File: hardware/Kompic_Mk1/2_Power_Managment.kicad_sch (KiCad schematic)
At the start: 32 parts, among them SW1 SKSCLBE010, U16 TPS62840DLCR, U2 XC6206P182MR, U4 BQ25619RTWR

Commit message: Added Circuit page! Minor touchups to schematic + Schematic PDF.
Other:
- company: Ivan Porupski May2026(c) -> Ivan Porupski June2026(c)
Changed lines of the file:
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@@
 	(paper "A4")
 	(title_block
-		(date "2026-05-30")
-		(rev "iv7.0")
-		(company "Ivan Porupski May2026(c)")
+		(date "2026-06-02")
+		(rev "iv7.1")
+		(company "Ivan Porupski June2026(c)")
 	)
 	(text "right at pin"

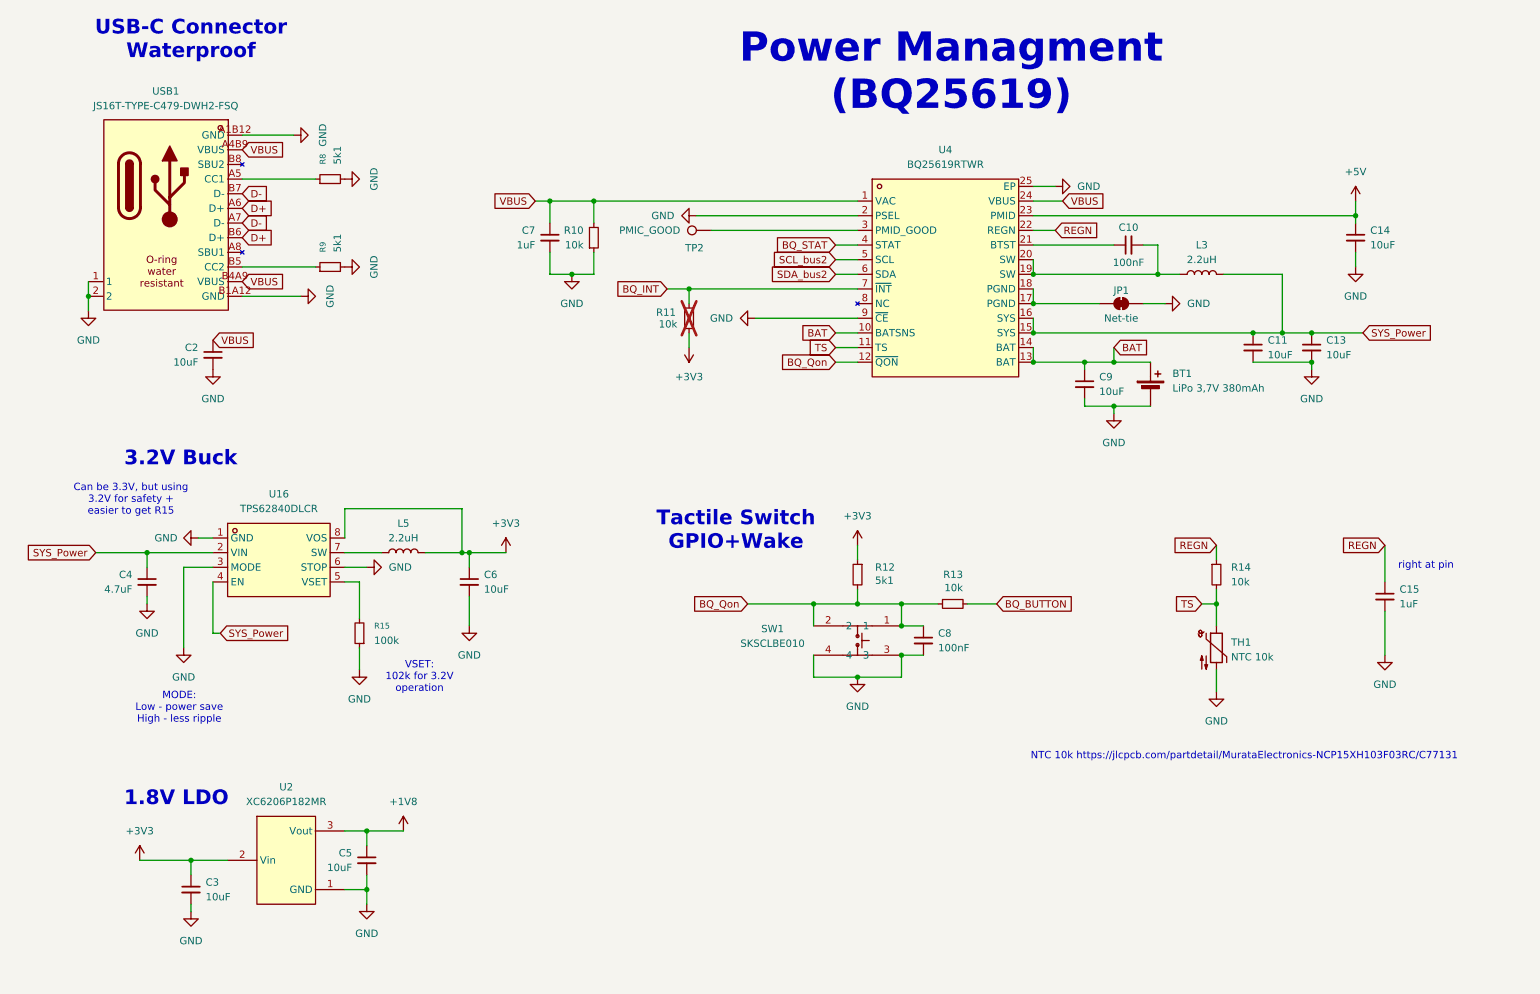
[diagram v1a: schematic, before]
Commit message: MASSIVE UPDATE: Built a working prototype with most systems go! iv7.1 requires about half a dozen surgical hacks on the PCB itself - it is suggested you wait for iv7.2+ - but otherwise, a massive success!
Stage 1-3 documents how the parts were added, in what fashion and then tested both electrically and with the scripts in test/ for each stage. SD Card may be unfixable in iv7.1.

Added notes where the bugs are in the schematic, but haven't updated it.
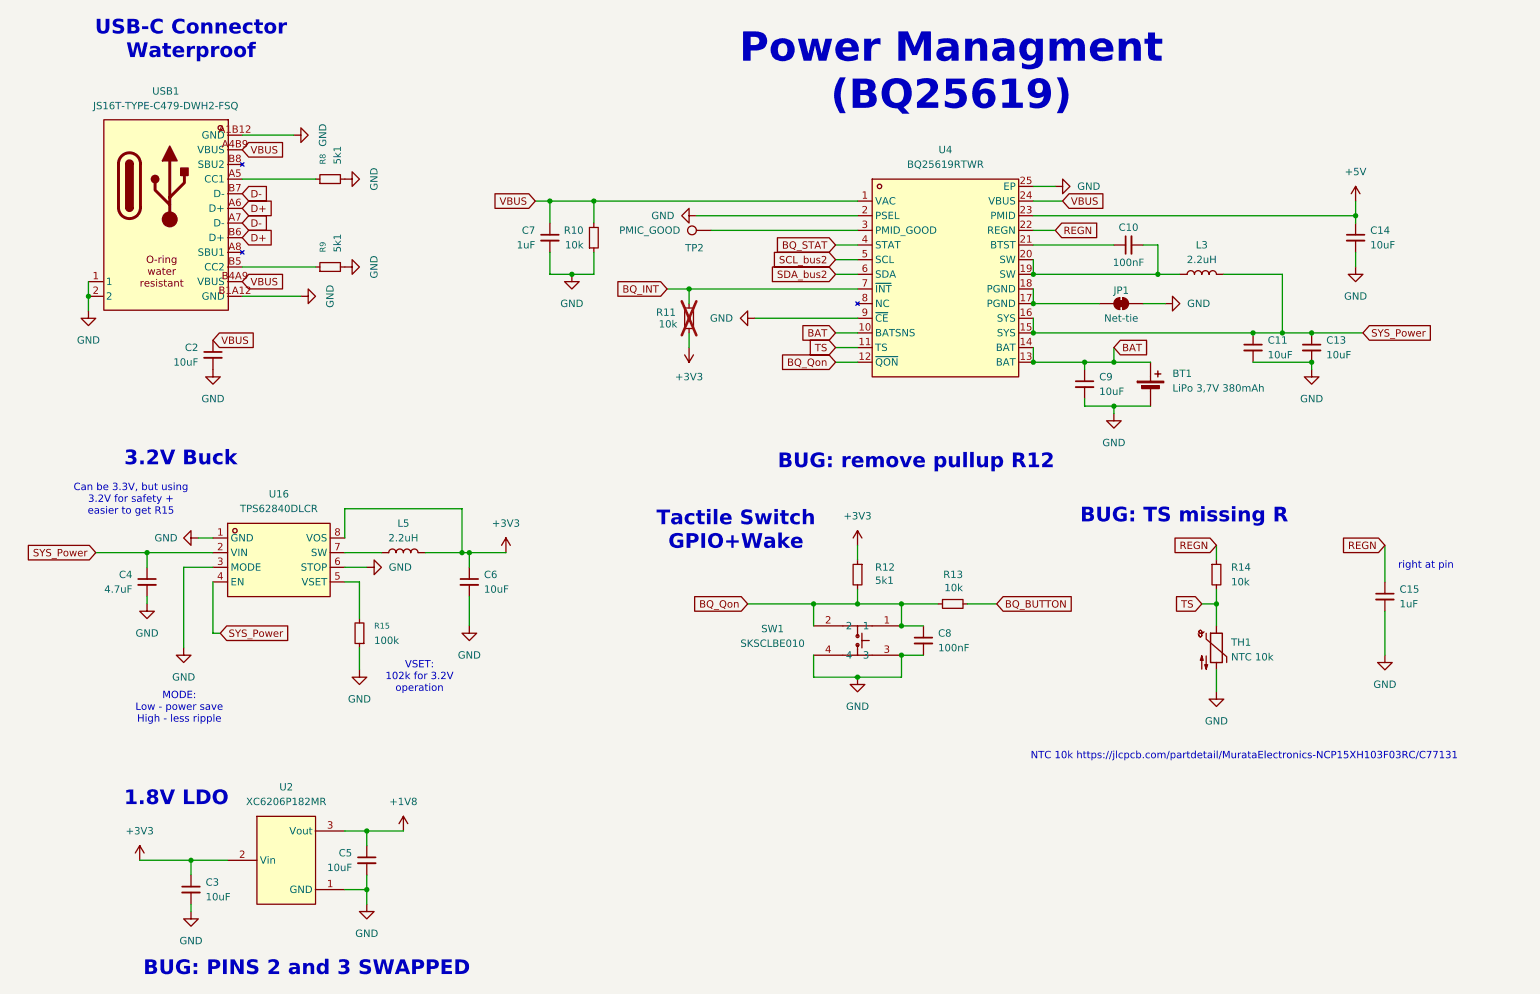
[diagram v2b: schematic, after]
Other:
- note added: "BUG: PINS 2 and 3 SWAPPED"
- note added: "BUG: TS missing R"
- note added: "BUG: remove pullup R12"
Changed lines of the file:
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@@
+		)
+	)
+	(text "BUG: remove pullup R12"
+		(exclude_from_sim no)
+		(at 173.99 103.632 0)
+		(effects
+			(font
+				(size 2.54 2.54)
+				(thickness 0.508)
+				(bold yes)
+				(color 255 38 26 1)
+			)
+		)
+	)
+	(text "BUG: TS missing R"
+		(exclude_from_sim no)
+		(at 220.472 113.03 0)
+		(effects
+			(font
+				(size 2.54 2.54)
+				(thickness 0.508)
+				(bold yes)
+				(color 255 38 26 1)
+			)
 		)
 	)
@@
 			)
 		)
+	)
+	(text "BUG: PINS 2 and 3 SWAPPED"
+		(exclude_from_sim no)
+		(at 68.326 191.516 0)
+		(effects
+			(font
+				(size 2.54 2.54)
+				(thickness 0.508)
+				(bold yes)
+				(color 255 38 26 1)
+			)
+		)
